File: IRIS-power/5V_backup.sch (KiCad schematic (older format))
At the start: 17 parts

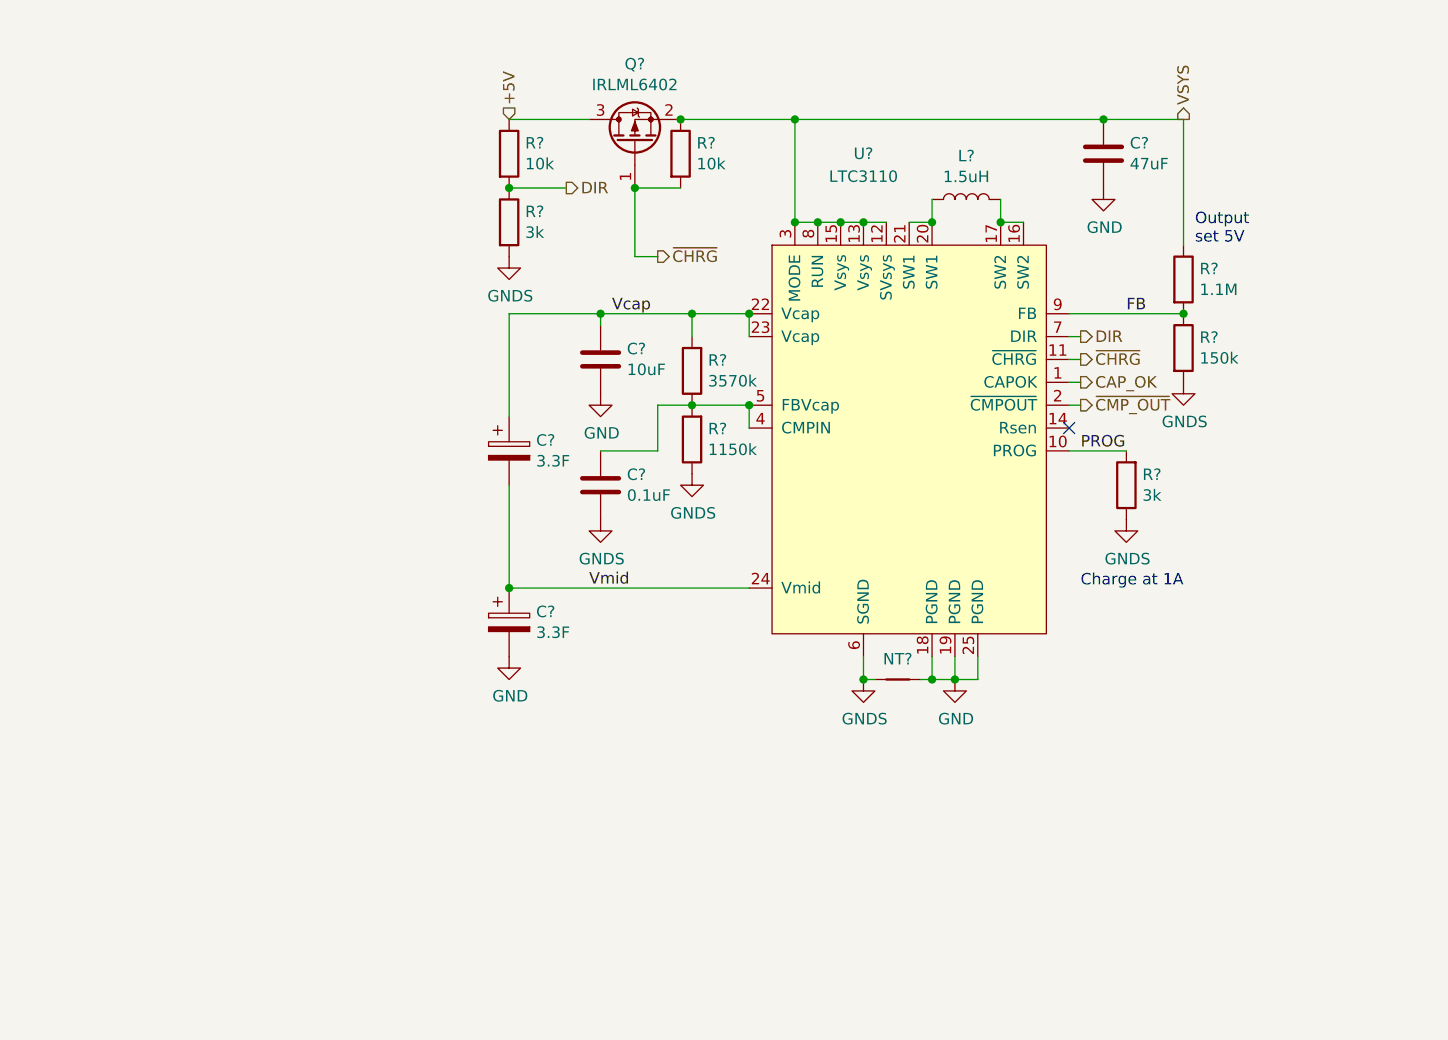
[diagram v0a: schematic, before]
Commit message: Finalized power board V2 schematic, preparing to layout
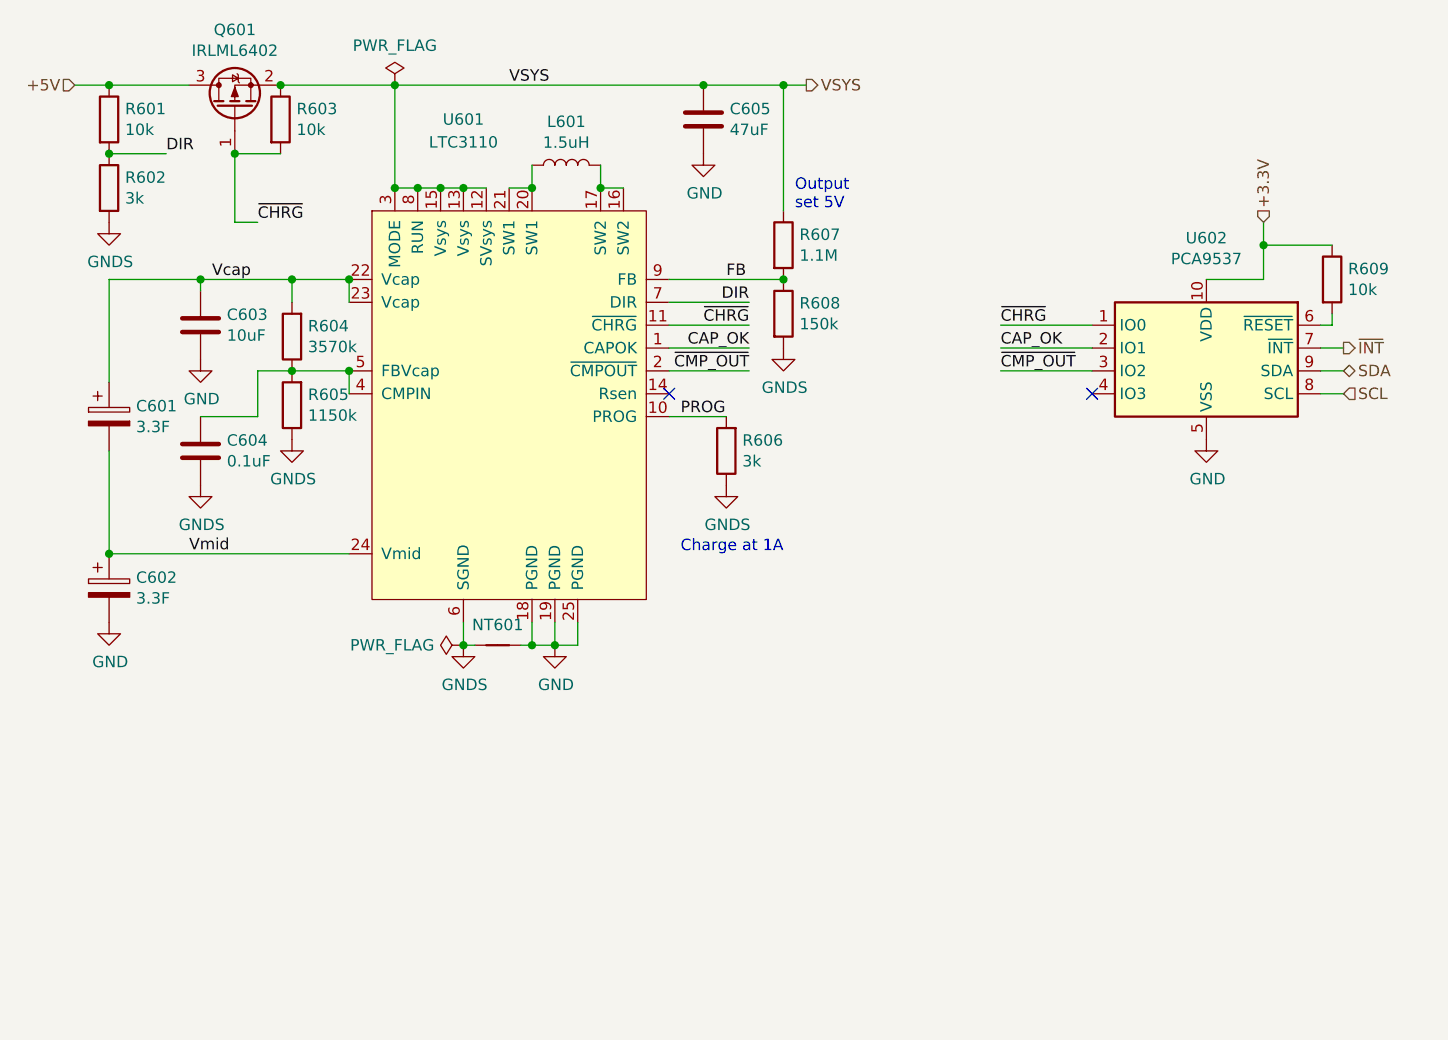
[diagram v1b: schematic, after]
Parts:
- added R609: 10k, Resistor_SMD:R_0603_1608Metric, symbol Device:R
- added U602: PCA9537, Package_SO:TSSOP-10_3x3mm_P0.5mm, symbol Interface_Expansion:PCA9537
- C601, C602: renamed from C?; footprint STARpower:SCCR20B335PRB -> star-common-lib:SCCR20B335PRB
- C603: renamed from C?; footprint Capacitor_SMD:C_1206_3216Metric -> Capacitor_SMD:C_0603_1608Metric
- C604: renamed from C?; footprint (none) -> Capacitor_SMD:C_0603_1608Metric
- C605: renamed from C?; footprint (none) -> Capacitor_SMD:C_1210_3225Metric
- L601: renamed from L?; footprint (none) -> star-common-lib:744316150; Digikey PN (none) -> 732-6178-1-ND; MFG PN (none) -> 744316150; Unit Cost (none) -> 2.55
- NT601: renamed from NT?; footprint (none) -> NetTie:NetTie-2_SMD_Pad0.5mm
- R601, R602, R603, R604, R605, R606: renamed from R?; footprint (none) -> Resistor_SMD:R_0603_1608Metric
- U601: renamed from U?; footprint (none) -> star-common-lib:LTC3110
- gave numbers to parts that had none: 3
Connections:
- net CAP_OK: now also U602.2 (IO1)
- net GND: now also U602.5 (VSS)
- net ~CHRG: now also U602.1 (IO0)
- net ~CMP_OUT: now also U602.3 (IO2)
- new net: R609.2, U602.6 (~RESET)
- new net +3.3V: R609.1, U602.10 (VDD)
- new net SCL: U602.8 (SCL)
- new net SDA: U602.9 (SDA)
- new net ~INT: U602.7 (~INT)
- no-connect marks 1 -> 2
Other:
- moved on the sheet: C601, C602, C603, C604, C605, L601, NT601, Q601, R601, R602, R603, R604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

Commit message: Updated layout
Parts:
- C605: footprint Capacitor_SMD:C_1210_3225Metric -> Capacitor_SMD:C_1206_3216Metric
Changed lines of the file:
@@
 F 0 "C605" H 5415 2996 50  0000 L CNN
 F 1 "47uF" H 5415 2905 50  0000 L CNN
-F 2 "Capacitor_SMD:C_1210_3225Metric" H 5338 2800 50  0001 C CNN
+F 2 "Capacitor_SMD:C_1206_3216Metric" H 5338 2800 50  0001 C CNN
 F 3 "~" H 5300 2950 50  0001 C CNN
 	1    5300 2950
@@
 Connection ~ 2700 2800
 $Comp
-L power:PWR_FLAG #FLG0105
+L power:PWR_FLAG #FLG0601
 U 1 1 5F36028E
 P 3950 2800
-F 0 "#FLG0105" H 3950 2875 50  0001 C CNN
+F 0 "#FLG0601" H 3950 2875 50  0001 C CNN
 F 1 "PWR_FLAG" H 3950 2973 50  0000 C CNN
 F 2 "" H 3950 2800 50  0001 C CNN
@@
 $EndComp
 $Comp
-L power:PWR_FLAG #FLG0106
+L power:PWR_FLAG #FLG0602
 U 1 1 5F360B80
 P 4250 5250
-F 0 "#FLG0106" H 4250 5325 50  0001 C CNN
+F 0 "#FLG0602" H 4250 5325 50  0001 C CNN
 F 1 "PWR_FLAG" V 4250 5377 50  0000 L CNN
 F 2 "" H 4250 5250 50  0001 C CNN

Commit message: Updated layout
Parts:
- added TP61: Vcap, TestPoint:TestPoint_Keystone_5000-5004_Miniature, symbol Connector:TestPoint_Probe
- renumbered C601 to C61, C602 to C62, C603 to C63, C604 to C64, C605 to C65, L601 to L61, NT601 to NT61, Q601 to Q61, R601 to R61, R602 to R62, R603 to R63, R604 to R64, R605 to R65, R606 to R66, R607 to R67, R608 to R68, R609 to R69, U601 to U61, U602 to U62
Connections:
- net Vcap: now also TP61.1
- net FBVcap: now reaches C64.1, R64.1, R65.2, U61.4 (CMPIN), U61.5 (FBVcap)
- net SW1: now reaches L61.1, U61.20 (SW1), U61.21 (SW1)
- net SW2: now reaches L61.2, U61.16 (SW2), U61.17 (SW2)

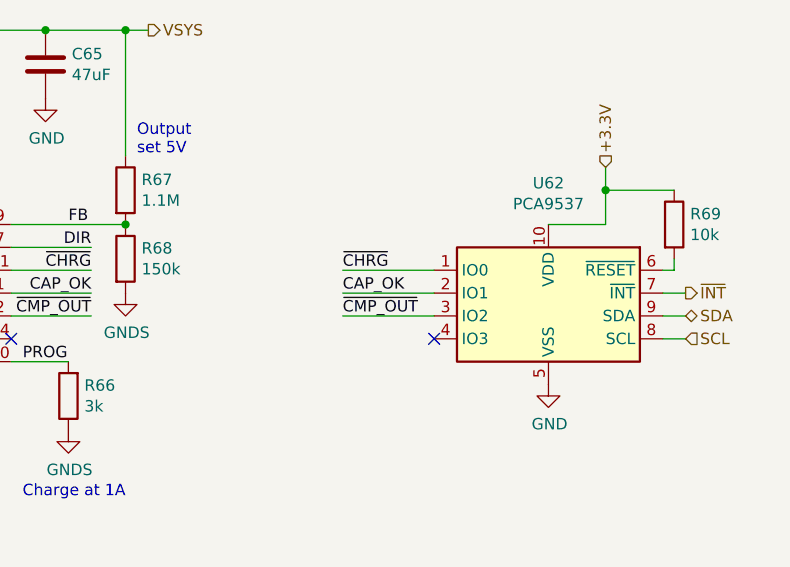
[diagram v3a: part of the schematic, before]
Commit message: Finished initial layout without gnd plane
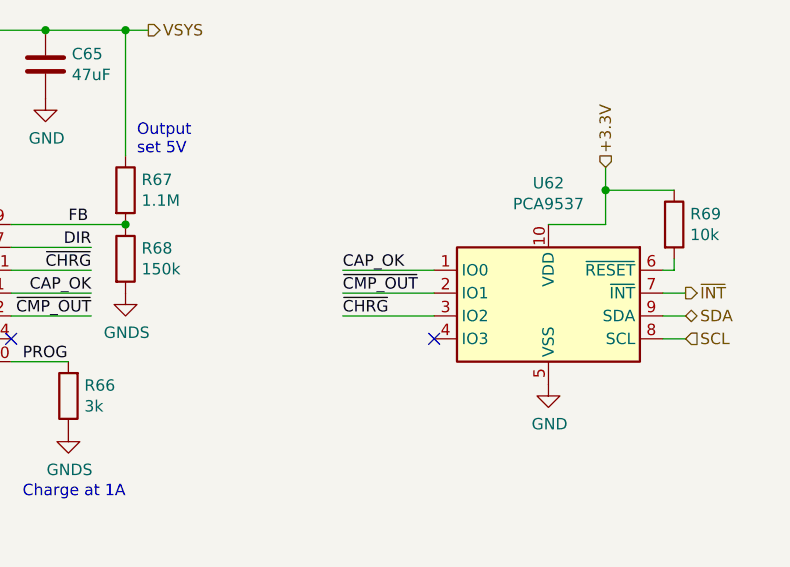
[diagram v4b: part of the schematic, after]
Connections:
- net CAP_OK: now also U62.1 (IO0); no longer U62.2 (IO1)
- net ~CHRG: now also U62.3 (IO2); no longer U62.1 (IO0)
- net ~CMP_OUT: now also U62.2 (IO1); no longer U62.3 (IO2)
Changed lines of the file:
@@
 Text Label 4450 2800 0    50   ~ 0
 VSYS
+Text Label 6600 4050 0    50   ~ 0
+~CHRG
 Text Label 6600 3850 0    50   ~ 0
-~CHRG
+CAP_OK
 Text Label 6600 3950 0    50   ~ 0
-CAP_OK
-Text Label 6600 4050 0    50   ~ 0
 ~CMP_OUT
 Wire Wire Line
@@
 NoConn ~ 7000 4150
 Wire Wire Line
-	7000 3850 6600 3850
+	7000 4050 6600 4050
 Wire Wire Line
-	6600 3950 7000 3950
+	6600 3850 7000 3850
 Wire Wire Line
-	7000 4050 6600 4050
+	7000 3950 6600 3950
 $Comp
 L Interface_Expansion:PCA9537 U62

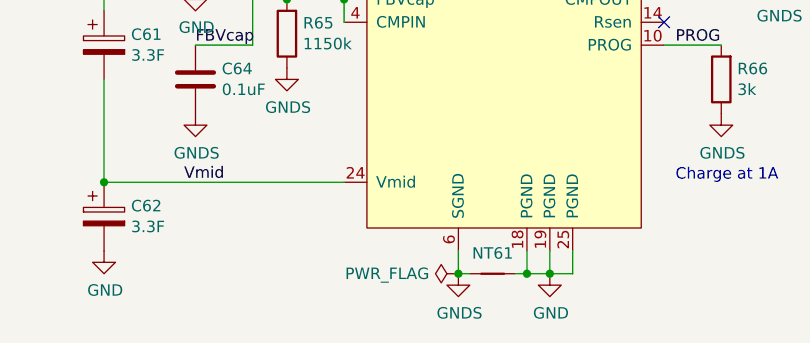
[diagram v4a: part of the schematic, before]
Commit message: Added some 3D models
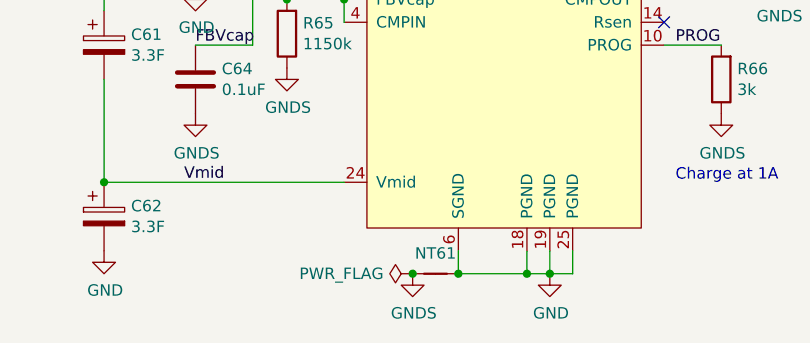
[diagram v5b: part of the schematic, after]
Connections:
- net GND: now also U61.6 (SGND)
- net GNDS: no longer U61.6 (SGND)
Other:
- moved on the sheet: NT61
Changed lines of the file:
@@
 L Device:Net-Tie_2 NT?
 U 1 1 5F4555AF
-P 4400 5250
+P 4150 5250
 AR Path="/5F4555AF" Ref="NT?"  Part="1"
 AR Path="/5F41BCFC/5F4555AF" Ref="NT61"  Part="1"
-F 0 "NT61" H 4400 5339 50  0000 C CNN
-F 1 "Net-Tie_2" H 4400 5340 50  0001 C CNN
-F 2 "NetTie:NetTie-2_SMD_Pad0.5mm" H 4400 5250 50  0001 C CNN
-F 3 "~" H 4400 5250 50  0001 C CNN
-	1    4400 5250
-	1    0    0    -1
-$EndComp
-Wire Wire Line
-	4500 5250 4550 5250
+F 0 "NT61" H 4150 5339 50  0000 C CNN
+F 1 "Net-Tie_2" H 4150 5340 50  0001 C CNN
+F 2 "NetTie:NetTie-2_SMD_Pad0.5mm" H 4150 5250 50  0001 C CNN
+F 3 "~" H 4150 5250 50  0001 C CNN
+	1    4150 5250
+	1    0    0    -1
+$EndComp
 Wire Wire Line
 	4550 5250 4550 5150
-Wire Wire Line
-	4300 5250 4250 5250
 Wire Wire Line
 	4250 5250 4250 5150
@@
 L power:GNDS #PWR?
 U 1 1 5F4555D1
-P 4250 5250
+P 4050 5250
 AR Path="/5F4555D1" Ref="#PWR?"  Part="1"
 AR Path="/5F41BCFC/5F4555D1" Ref="#PWR066"  Part="1"
-F 0 "#PWR066" H 4250 5000 50  0001 C CNN
-F 1 "GNDS" H 4255 5077 50  0000 C CNN
-F 2 "" H 4250 5250 50  0001 C CNN
-F 3 "" H 4250 5250 50  0001 C CNN
-	1    4250 5250
-	1    0    0    -1
-$EndComp
-Connection ~ 4250 5250
+F 0 "#PWR066" H 4050 5000 50  0001 C CNN
+F 1 "GNDS" H 4055 5077 50  0000 C CNN
+F 2 "" H 4050 5250 50  0001 C CNN
+F 3 "" H 4050 5250 50  0001 C CNN
+	1    4050 5250
+	1    0    0    -1
+$EndComp
 $Comp
 L power:GNDS #PWR?
@@
 L power:PWR_FLAG #FLG062
 U 1 1 5F360B80
-P 4250 5250
-F 0 "#FLG062" H 4250 5325 50  0001 C CNN
-F 1 "PWR_FLAG" V 4250 5377 50  0000 L CNN
-F 2 "" H 4250 5250 50  0001 C CNN
-F 3 "~" H 4250 5250 50  0001 C CNN
-	1    4250 5250
+P 4050 5250
+F 0 "#FLG062" H 4050 5325 50  0001 C CNN
+F 1 "PWR_FLAG" V 4050 5377 50  0000 L CNN
+F 2 "" H 4050 5250 50  0001 C CNN
+F 3 "~" H 4050 5250 50  0001 C CNN
+	1    4050 5250
 	0    -1   -1   0
 $EndComp
@@
 Wire Wire Line
 	3100 3550 3100 3650
+Wire Wire Line
+	4250 5250 4550 5250
+Connection ~ 4250 5250
+Connection ~ 4050 5250
 $EndSCHEMATC

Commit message: Begin revising for IRIS V4
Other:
- note added: "1A"
- note added: "2.42V"
- note added: "2.66V"
- note added: "4.494V"
- note added: "5.0V"
- note added: "CURRENT VALUE"
- note added: "Charge Current Lim = 3kOhm/R66"
- note added: "FORMULA"
- note added: "Vcap = (1.095) * (1 + R64/R65)"
- note added: "Vsys = 0.6 * (1 + R67/R68)"
- note added: "Vth(falling) = 0.59 * (1 + R64/65)"
- note added: "Vth(rising) = 0.65 * (1 + R64/R65)"
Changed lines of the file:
@@
 Connection ~ 4250 5250
 Connection ~ 4050 5250
+Text Notes 3650 5850 0    50   ~ 0
+FORMULA
+Text Notes 4700 5850 0    50   ~ 0
+CURRENT VALUE
+Wire Notes Line
+	3150 5900 5400 5900
+Wire Notes Line
+	3150 6100 5400 6100
+Text Notes 4900 6050 0    50   ~ 0
+4.494V
+Wire Notes Line
+	3150 6300 5400 6300
+Text Notes 3200 6250 0    50   ~ 0
+Vsys = 0.6 * (1 + R67/R68)
+Text Notes 3200 6050 0    50   ~ 0
+Vcap = (1.095) * (1 + R64/R65)
+Text Notes 4900 6250 0    50   ~ 0
+5.0V
+Wire Notes Line
+	3150 6500 5400 6500
+Wire Notes Line
+	3150 6700 5400 6700
+Text Notes 3200 6450 0    50   ~ 0
+Charge Current Lim = 3kOhm/R66
+Text Notes 4950 6450 0    50   ~ 0
+1A
+Text Notes 3200 6650 0    50   ~ 0
+Vth(rising) = 0.65 * (1 + R64/R65)
+Text Notes 3200 6850 0    50   ~ 0
+Vth(falling) = 0.59 * (1 + R64/65)
+Text Notes 4900 6650 0    50   ~ 0
+2.66V
+Text Notes 4900 6850 0    50   ~ 0
+2.42V
+Wire Notes Line
+	4650 6900 4650 5700
+Wire Notes Line
+	3150 5700 3150 6900
+Wire Notes Line
+	3150 6900 5400 6900
+Wire Notes Line
+	5400 6900 5400 5700
+Wire Notes Line
+	3150 5700 5400 5700
 $EndSCHEMATC

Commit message: Updated IRIS power board for V4
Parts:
- C61, C62: footprint star-common-lib:SCCR20B335PRB -> star-common-lib:CAP_10x27_5mm_pitch
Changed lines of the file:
@@
 F 0 "C61" H 2818 4296 50  0000 L CNN
 F 1 "3.3F" H 2818 4205 50  0000 L CNN
-F 2 "star-common-lib:SCCR20B335PRB" H 2738 4100 50  0001 C CNN
+F 2 "star-common-lib:CAP_10x27_5mm_pitch" H 2738 4100 50  0001 C CNN
 F 3 "SCCR20B335PRB" H 2700 4250 50  0001 C CNN
 	1    2700 4250
@@
 F 0 "C62" H 2818 5046 50  0000 L CNN
 F 1 "3.3F" H 2818 4955 50  0000 L CNN
-F 2 "star-common-lib:SCCR20B335PRB" H 2738 4850 50  0001 C CNN
+F 2 "star-common-lib:CAP_10x27_5mm_pitch" H 2738 4850 50  0001 C CNN
 F 3 "SCCR20B335PRB" H 2700 5000 50  0001 C CNN
 	1    2700 5000

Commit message: Improved fuel gauge layout
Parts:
- C61, C62: Digikey PN (none) -> 1572-DGH106Q2R7C-ND
- C63: Digikey PN (none) -> 1276-1192-1-ND
- C64: Digikey PN (none) -> 1276-CL10B104KB8NNNLCT-ND
- C65: Digikey PN (none) -> 1276-3063-1-ND
- R61, R63, R69: Digikey PN (none) -> RNCP0603FTD10K0CT-ND
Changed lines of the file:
@@
 F 2 "Capacitor_SMD:C_0603_1608Metric" H 3138 4250 50  0001 C CNN
 F 3 "~" H 3100 4400 50  0001 C CNN
+F 4 "1276-CL10B104KB8NNNLCT-ND" H 3100 4400 50  0001 C CNN "Digikey PN"
 	1    3100 4400
 	1    0    0    -1
@@
 F 1 "3.3F" H 2818 4205 50  0000 L CNN
 F 2 "star-common-lib:CAP_10x27_5mm_pitch" H 2738 4100 50  0001 C CNN
-F 3 "SCCR20B335PRB" H 2700 4250 50  0001 C CNN
+F 3 "" H 2700 4250 50  0001 C CNN
+F 4 "1572-DGH106Q2R7C-ND" H 2700 4250 50  0001 C CNN "Digikey PN"
 	1    2700 4250
 	1    0    0    -1
@@
 F 1 "3.3F" H 2818 4955 50  0000 L CNN
 F 2 "star-common-lib:CAP_10x27_5mm_pitch" H 2738 4850 50  0001 C CNN
-F 3 "SCCR20B335PRB" H 2700 5000 50  0001 C CNN
+F 3 "" H 2700 5000 50  0001 C CNN
+F 4 "1572-DGH106Q2R7C-ND" H 2700 5000 50  0001 C CNN "Digikey PN"
 	1    2700 5000
 	1    0    0    -1
@@
 F 2 "Capacitor_SMD:C_0603_1608Metric" H 3138 3700 50  0001 C CNN
 F 3 "~" H 3100 3850 50  0001 C CNN
+F 4 "1276-1192-1-ND" H 3100 3850 50  0001 C CNN "Digikey PN"
 	1    3100 3850
 	1    0    0    -1
@@
 F 2 "Resistor_SMD:R_0603_1608Metric" V 2630 2950 50  0001 C CNN
 F 3 "~" H 2700 2950 50  0001 C CNN
+F 4 "RNCP0603FTD10K0CT-ND" H 2700 2950 50  0001 C CNN "Digikey PN"
 	1    2700 2950
 	1    0    0    -1
@@
 F 2 "Resistor_SMD:R_0603_1608Metric" V 3380 2950 50  0001 C CNN
 F 3 "~" H 3450 2950 50  0001 C CNN
+F 4 "RNCP0603FTD10K0CT-ND" H 3450 2950 50  0001 C CNN "Digikey PN"
 	1    3450 2950
 	1    0    0    -1
@@
 F 2 "Capacitor_SMD:C_1206_3216Metric" H 5338 2800 50  0001 C CNN
 F 3 "~" H 5300 2950 50  0001 C CNN
+F 4 "1276-3063-1-ND" H 5300 2950 50  0001 C CNN "Digikey PN"
 	1    5300 2950
 	1    0    0    -1
@@
 F 2 "Resistor_SMD:R_0603_1608Metric" V 7980 3650 50  0001 C CNN
 F 3 "~" H 8050 3650 50  0001 C CNN
+F 4 "RNCP0603FTD10K0CT-ND" H 8050 3650 50  0001 C CNN "Digikey PN"
 	1    8050 3650
 	1    0    0    -1
